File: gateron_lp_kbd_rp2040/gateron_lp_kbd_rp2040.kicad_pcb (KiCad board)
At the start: 2 copper layers, 234.5 x 116.5 mm, 306 parts, among them J1 TYPE-C-31-M-12, J2 Battery JST-SH, Q1 DMG3415U, SW1 KS-33, SW10 KS-33, SW11 KS-33, SW12 KS-33, SW13 KS-33, SW14 KS-33, SW15 KS-33, SW16 KS-33, SW17 KS-33, SW18 KS-33, SW19 KS-33, SW2 KS-33, SW20 KS-33, SW21 KS-33, SW22 KS-33, SW23 KS-33, SW24 KS-33, SW25 KS-33, SW26 KS-33, SW27 KS-33, SW28 KS-33, SW29 KS-33, SW3 KS-33, SW30 KS-33, SW31 KS-33, SW32 KS-33, SW33 KS-33, SW34 KS-33, SW35 KS-33, SW36 KS-33, SW37 KS-33, SW38 KS-33, SW39 KS-33, SW4 KS-33, SW40 KS-33, SW41 KS-33, SW42 KS-33, SW43 KS-33, SW44 KS-33, SW45 KS-33, SW46 KS-33, SW47 KS-33, SW48 KS-33, SW49 KS-33, SW5 KS-33, SW50 KS-33, SW51 KS-33, SW52 KS-33, SW53 KS-33, SW54 KS-33, SW55 KS-33, SW56 KS-33, SW57 KS-33, SW58 KS-33, SW59 KS-33, SW6 KS-33, SW60 RESET, SW61 BOOTSEL, SW62 PWR MSK-12C02, SW7 KS-33, SW8 KS-33, SW9 KS-33, U1 RP2040, U2 MCP73831, U3 AP2112K-3.3, U4 USBLC6-2SC6, U5 W25Q16JVUXIQ, U6 CYW43439, U7 SN74AHCT1G125DBVR, Y1 12MHz, Y2 37.4MHz

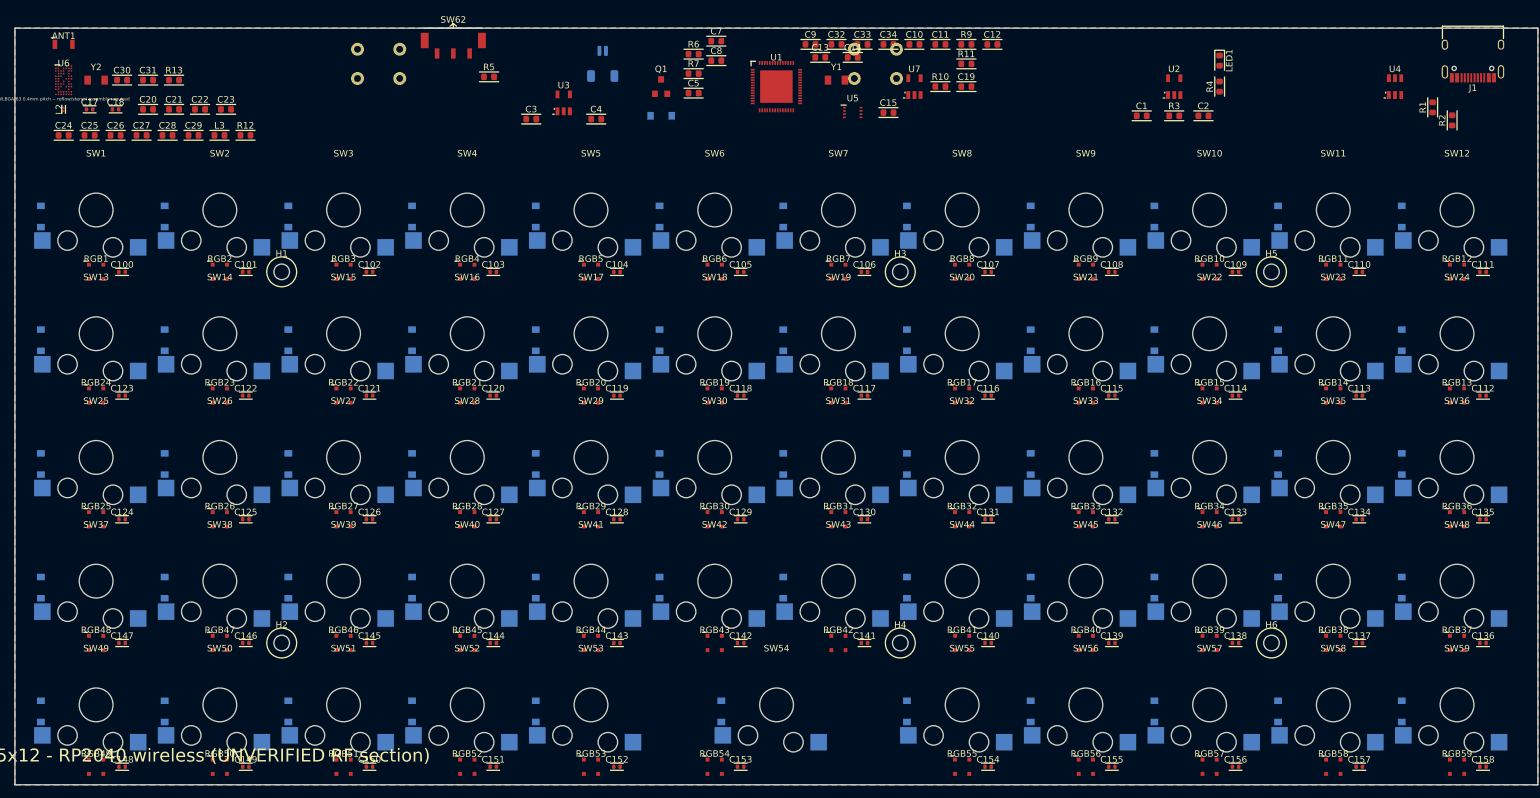
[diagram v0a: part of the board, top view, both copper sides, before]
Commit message: Add RP2040 board routing engine, reverse-mount LED redesign, and 3D models
- New route_kbd_rp2040.py: deterministic + A*-hybrid autorouter for the
  RP2040 variant. Hand-routes the congested ROW/COL matrix fanout and
  QSPI north strip net-by-net (verified against the real clearance
  checker), falls back to generic A* elsewhere, and heals remaining
  gaps in a final pass.
- Redesigned the per-key RGB LED footprint (fp_sk6812mini) to a real
  reverse-mount part on B.Cu with a light-transmission cutout, matching
  a verified KiCad reference footprint instead of a hand-derived one.
- Added 3D models to ~15 footprints across both board variants (via
  add_3d.py for the ESP32 variant, inline `model()` blocks for RP2040)
  and synced datasheets for real part verification.
- Fixed several real bugs surfaced while routing: VSYS's per-LED
  routing referenced the wrong pin after the LED footprint redesign
  (silently trying to via into GND on all 59 LEDs); the matching
  per-LED decoupling caps sat in the ~0mm gap between the LED's own
  cutout and the next row's switch leg hole; C33 was placed closer to
  BOOTSEL's through-hole pad than any trace could legally clear;
  BOOTSEL's own switch had two same-named leg pads that were never
  wired together; VBAT_SENSE's escape route was getting walled off by
  whichever of XIN/XOUT happened to route first.
- Board currently routes cleanly except for a known cluster of nets
  (+3V3, DVDD, QSPI_SCLK/SD2/SD3, RGB_GPIO, USB_DM/DP, VREG_VIN) all
  bottlenecked by the same over-saturated escape corridor next to U1 --
  next up for a dedicated deterministic-routing pass.

Co-Authored-By: Claude Sonnet 5 <noreply@anthropic.com>
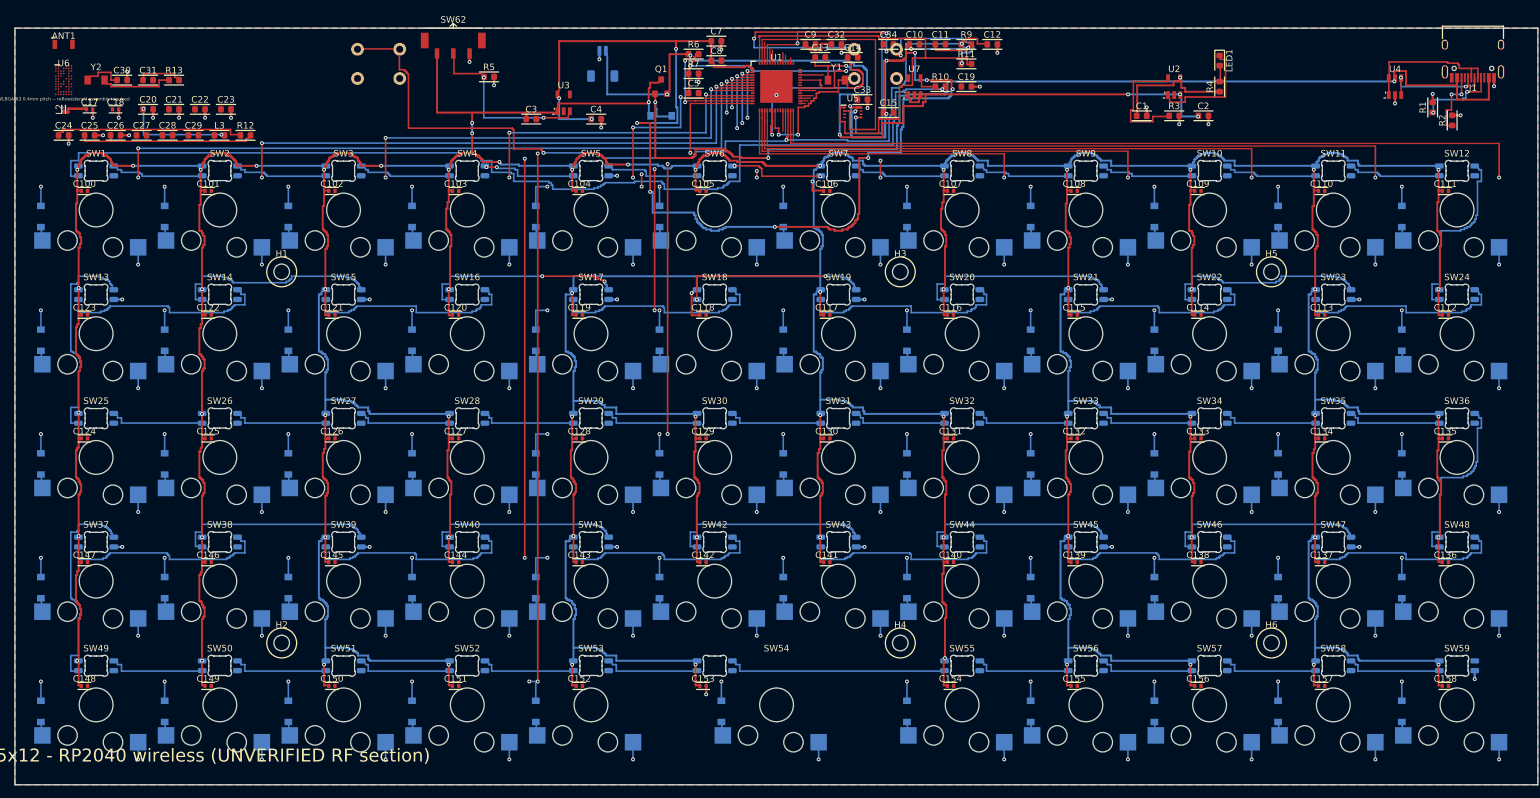
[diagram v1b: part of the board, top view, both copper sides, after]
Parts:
- RGB1, RGB10, RGB11, RGB12, RGB13, RGB14, RGB15, RGB16, RGB17, RGB18, RGB19, RGB2, RGB20, RGB21, RGB22, RGB23, RGB24, RGB25, RGB26, RGB27, RGB28, RGB29, RGB3, RGB30, RGB31, RGB32, RGB33, RGB34, RGB35, RGB36, RGB37, RGB38, RGB39, RGB4, RGB40, RGB41, RGB42, RGB43, RGB44, RGB45, RGB46, RGB47, RGB48, RGB49, RGB5, RGB50, RGB51, RGB52, RGB53, RGB54, RGB55, RGB56, RGB57, RGB58, RGB59, RGB6, RGB7, RGB8, RGB9: moved to B.Cu
- moved RGB13 15.6 mm to (259.6, 63.0), turned to 180 degrees
- moved RGB14 15.6 mm to (240.5, 63.0), turned to 180 degrees
- moved RGB15 15.6 mm to (221.4, 63.0), turned to 180 degrees
- moved RGB16 15.6 mm to (202.4, 63.0), turned to 180 degrees
- moved RGB17 15.6 mm to (183.3, 63.0), turned to 180 degrees
- moved RGB18 15.6 mm to (164.3, 63.0), turned to 180 degrees
- moved RGB19 15.6 mm to (145.2, 63.0), turned to 180 degrees
- moved RGB20 15.6 mm to (126.2, 63.0), turned to 180 degrees
- moved RGB21 15.6 mm to (107.2, 63.0), turned to 180 degrees
- moved RGB22 15.6 mm to (88.1, 63.0), turned to 180 degrees
- moved RGB23 15.6 mm to (69.0, 63.0), turned to 180 degrees
- moved RGB24 15.6 mm to (50.0, 63.0), turned to 180 degrees
- moved RGB1 15.5 mm to (50.0, 44.0), turned to 180 degrees
- moved RGB10 15.5 mm to (221.4, 44.0), turned to 180 degrees
- moved RGB11 15.5 mm to (240.5, 44.0), turned to 180 degrees
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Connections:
- RGB1 pad 1: VSYS -> GND
- RGB1 pad 3: GND -> VSYS
- RGB10 pad 1: VSYS -> GND
- RGB10 pad 3: GND -> VSYS
- RGB11 pad 1: VSYS -> GND
- RGB11 pad 3: GND -> VSYS
- RGB12 pad 1: VSYS -> GND
- RGB12 pad 3: GND -> VSYS
- RGB13 pad 1: VSYS -> GND
- RGB13 pad 3: GND -> VSYS
- RGB14 pad 1: VSYS -> GND
- RGB14 pad 3: GND -> VSYS
- RGB15 pad 1: VSYS -> GND
- RGB15 pad 3: GND -> VSYS
- RGB16 pad 1: VSYS -> GND
- RGB16 pad 3: GND -> VSYS
- RGB17 pad 1: VSYS -> GND
- RGB17 pad 3: GND -> VSYS
- RGB18 pad 1: VSYS -> GND
- RGB18 pad 3: GND -> VSYS
- RGB19 pad 1: VSYS -> GND
- RGB19 pad 3: GND -> VSYS
- RGB2 pad 1: VSYS -> GND
- RGB2 pad 3: GND -> VSYS
- RGB20 pad 1: VSYS -> GND
- RGB20 pad 3: GND -> VSYS
- RGB21 pad 1: VSYS -> GND
- RGB21 pad 3: GND -> VSYS
- RGB22 pad 1: VSYS -> GND
- RGB22 pad 3: GND -> VSYS
- RGB23 pad 1: VSYS -> GND
- RGB23 pad 3: GND -> VSYS
- RGB24 pad 1: VSYS -> GND
- RGB24 pad 3: GND -> VSYS
- RGB25 pad 1: VSYS -> GND
- RGB25 pad 3: GND -> VSYS
- RGB26 pad 1: VSYS -> GND
- RGB26 pad 3: GND -> VSYS
- RGB27 pad 1: VSYS -> GND
- RGB27 pad 3: GND -> VSYS
- RGB28 pad 1: VSYS -> GND
- RGB28 pad 3: GND -> VSYS
- RGB29 pad 1: VSYS -> GND
- RGB29 pad 3: GND -> VSYS
- RGB3 pad 1: VSYS -> GND
- RGB3 pad 3: GND -> VSYS
- RGB30 pad 1: VSYS -> GND
- RGB30 pad 3: GND -> VSYS
- RGB31 pad 1: VSYS -> GND
- RGB31 pad 3: GND -> VSYS
- RGB32 pad 1: VSYS -> GND
- RGB32 pad 3: GND -> VSYS
- RGB33 pad 1: VSYS -> GND
- RGB33 pad 3: GND -> VSYS
- RGB34 pad 1: VSYS -> GND
- RGB34 pad 3: GND -> VSYS
- RGB35 pad 1: VSYS -> GND
- RGB35 pad 3: GND -> VSYS
- RGB36 pad 1: VSYS -> GND
- RGB36 pad 3: GND -> VSYS
- RGB37 pad 1: VSYS -> GND
- RGB37 pad 3: GND -> VSYS
- RGB38 pad 1: VSYS -> GND
- RGB38 pad 3: GND -> VSYS
- RGB39 pad 1: VSYS -> GND
- RGB39 pad 3: GND -> VSYS
- RGB4 pad 1: VSYS -> GND
- RGB4 pad 3: GND -> VSYS
- RGB40 pad 1: VSYS -> GND
- RGB40 pad 3: GND -> VSYS
- RGB41 pad 1: VSYS -> GND
- RGB41 pad 3: GND -> VSYS
- RGB42 pad 1: VSYS -> GND
- RGB42 pad 3: GND -> VSYS
- RGB43 pad 1: VSYS -> GND
- RGB43 pad 3: GND -> VSYS
- RGB44 pad 1: VSYS -> GND
- RGB44 pad 3: GND -> VSYS
- RGB45 pad 1: VSYS -> GND
- RGB45 pad 3: GND -> VSYS
- RGB46 pad 1: VSYS -> GND
- RGB46 pad 3: GND -> VSYS
- RGB47 pad 1: VSYS -> GND
- RGB47 pad 3: GND -> VSYS
- RGB48 pad 1: VSYS -> GND
- RGB48 pad 3: GND -> VSYS
- RGB49 pad 1: VSYS -> GND
- RGB49 pad 3: GND -> VSYS
- RGB5 pad 1: VSYS -> GND
- RGB5 pad 3: GND -> VSYS
- RGB50 pad 1: VSYS -> GND
- RGB50 pad 3: GND -> VSYS
- RGB51 pad 1: VSYS -> GND
- RGB51 pad 3: GND -> VSYS
- RGB52 pad 1: VSYS -> GND
- RGB52 pad 3: GND -> VSYS
- RGB53 pad 1: VSYS -> GND
- RGB53 pad 3: GND -> VSYS
- RGB54 pad 1: VSYS -> GND
- RGB54 pad 3: GND -> VSYS
- RGB55 pad 1: VSYS -> GND
- RGB55 pad 3: GND -> VSYS
- RGB56 pad 1: VSYS -> GND
- RGB56 pad 3: GND -> VSYS
- RGB57 pad 1: VSYS -> GND
- RGB57 pad 3: GND -> VSYS
- RGB58 pad 1: VSYS -> GND
- RGB58 pad 3: GND -> VSYS
- RGB59 pad 1: VSYS -> GND
- RGB59 pad 3: GND -> VSYS
- RGB6 pad 1: VSYS -> GND
- RGB6 pad 3: GND -> VSYS
- RGB7 pad 1: VSYS -> GND
- RGB7 pad 3: GND -> VSYS
- RGB8 pad 1: VSYS -> GND
- RGB8 pad 3: GND -> VSYS
- RGB9 pad 1: VSYS -> GND
- RGB9 pad 3: GND -> VSYS
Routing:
- net VSYS: track 0.00 -> 1444.5 mm, vias 0 -> 68
- net ROW4: track 0.00 -> 368.9 mm, vias 0 -> 15
- net ROW3: track 0.00 -> 356.0 mm, vias 0 -> 16
- net ROW2: track 0.00 -> 315.3 mm, vias 0 -> 16
- net ROW1: track 0.00 -> 298.7 mm, vias 0 -> 16
- net ROW0: track 0.00 -> 282.0 mm, vias 0 -> 16
- net +3V3: track 0.00 -> 243.5 mm, vias 0 -> 16
- net COL11: track 0.00 -> 222.3 mm, vias 0 -> 6
- net COL0: track 0.00 -> 212.1 mm, vias 0 -> 8
- net COL10: track 0.00 -> 206.8 mm, vias 0 -> 6
- net COL1: track 0.00 -> 192.6 mm, vias 0 -> 8
- net COL9: track 0.00 -> 188.2 mm, vias 0 -> 6
- net VBUS: track 0.00 -> 186.7 mm, vias 0 -> 4
- net COL2: track 0.00 -> 173.2 mm, vias 0 -> 8
- net COL8: track 0.00 -> 169.5 mm, vias 0 -> 6
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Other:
- copper layers 2 -> 4

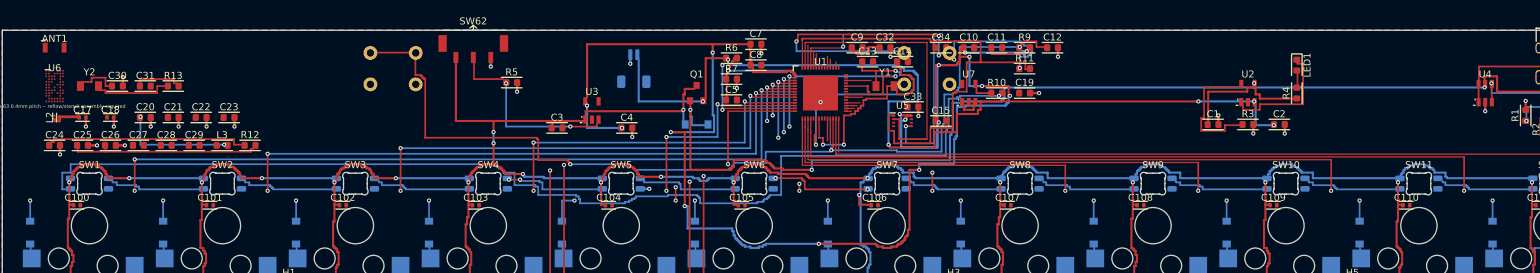
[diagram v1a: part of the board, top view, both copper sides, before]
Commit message: Route +3V3/DVDD orphan pins via In1/In2 expressways
Fixes 7 of 8 remaining +3V3/DVDD U1-pin orphans (pins 10, 22, 33, 42,
43, 48, 49, and DVDD pin 23) by hand-placing short F-layer escape jogs
into In1/In2 highway crossings instead of relying on the generic A*
router, which kept losing to 0.4mm-pitch pin congestion near U1.

+3V3 is now fully connected. DVDD's C32->C33 hop and pin 10's own long
F-layer escape wall still need work -- the latter is currently
trapping XIN's and QSPI_SS's own escape routes (regression, still
being chased).

Co-Authored-By: Claude Sonnet 5 <noreply@anthropic.com>
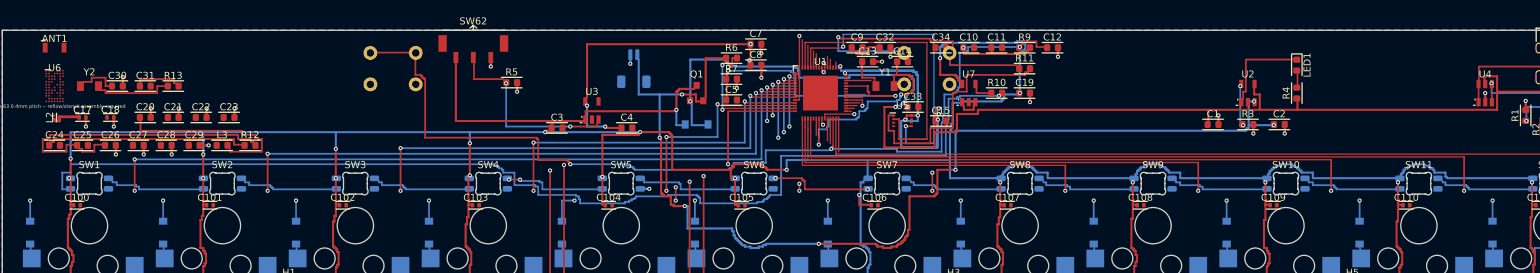
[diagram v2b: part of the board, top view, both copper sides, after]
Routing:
- net VSYS: track 1444.5 -> 1512.8 mm, vias 68 -> 69
- net XIN: track 40.0 -> 7.30 mm, vias 2 -> 0
- net QSPI_SS: track 71.1 -> 39.1 mm
- net BAT+: track 133.0 -> 157.2 mm, vias 6 -> 7
- net BOOTSEL: track 63.5 -> 41.5 mm, vias 5 -> 1
- net CYW_PA_VDD: track 27.9 -> 45.0 mm
- net DVDD: track 5.33 -> 18.9 mm, vias 0 -> 2
- net PROG: track 18.7 -> 6.13 mm, vias 0 -> 2
- net CYW_VDD1P5: track 16.3 -> 27.5 mm, vias 2 -> 0
- net +3V3: track 243.5 -> 235.3 mm, vias 16 -> 17
- net STAT: track 17.3 -> 13.5 mm
- net VBUS: track 186.7 -> 189.1 mm, vias 4 -> 2
- net XOUT: track 33.4 -> 34.0 mm

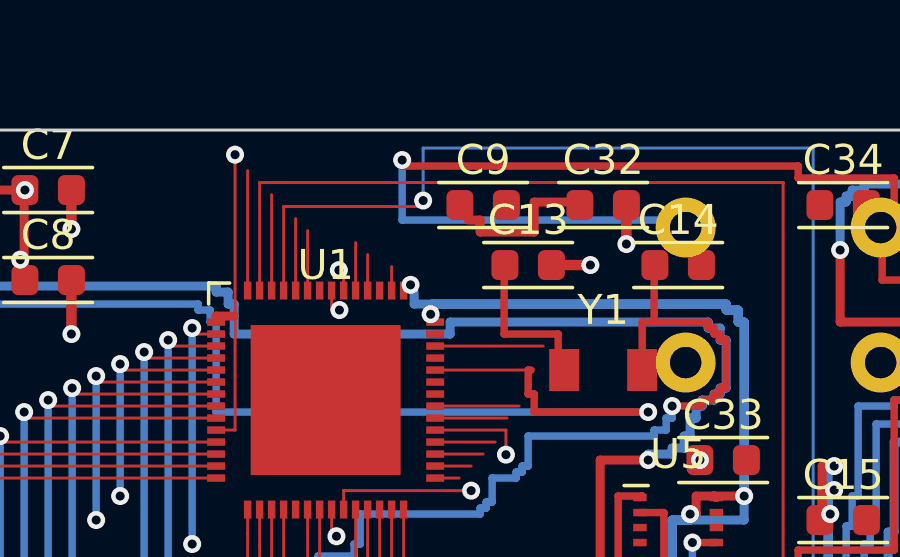
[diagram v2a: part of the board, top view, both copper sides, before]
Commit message: Fix DVDD's C33->U1 pins 45/50 hop, completing the +3V3/DVDD refactor
The direct route from C33's via to U1's N-side pins 45/50 crosses a
pocket (x=152-168, y=29-36) saturated with other nets' own vias
(+3V3, QSPI_SD0, VBAT_SENSE, XOUT, a GND keepout) -- no lane at any Y
in that band clears on any layer. Routed around it instead, joining
the existing C32->C33 In1 highway's y=23.5 lane at y=23.7 (23.5 itself
is blocked by a BOOTSEL via 0.5mm away).

DVDD and +3V3 are now both fully connected.

Co-Authored-By: Claude Sonnet 5 <noreply@anthropic.com>
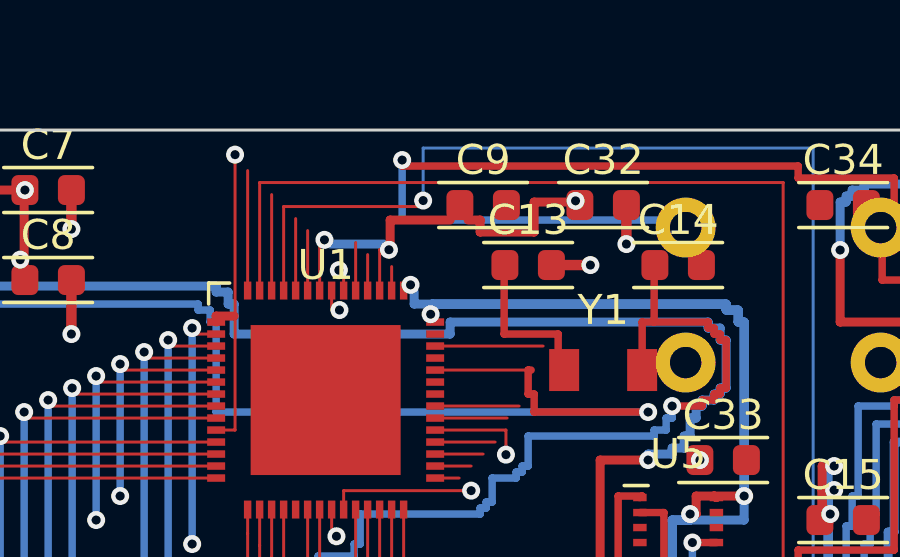
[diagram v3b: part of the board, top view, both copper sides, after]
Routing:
- net DVDD: track 18.9 -> 47.3 mm, vias 2 -> 5
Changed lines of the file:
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@@
   (segment (start 161.700 24.400) (end 163.300 24.400) (width 0.3) (layer "F.Cu") (net 18))
   (segment (start 163.225 24.500) (end 163.300 24.400) (width 0.3) (layer "F.Cu") (net 18))
+  (segment (start 163.225 24.500) (end 163.080 24.500) (width 0.1) (layer "F.Cu") (net 18))
+  (segment (start 163.080 24.500) (end 163.080 24.360) (width 0.1) (layer "F.Cu") (net 18))
+  (segment (start 163.080 24.360) (end 163.080 23.500) (width 0.3) (layer "In1.Cu") (net 18))
+  (segment (start 163.080 23.500) (end 170.000 23.500) (width 0.3) (layer "In1.Cu") (net 18))
+  (segment (start 170.000 23.500) (end 170.000 33.000) (width 0.3) (layer "In1.Cu") (net 18))
+  (segment (start 170.000 33.000) (end 167.225 33.000) (width 0.3) (layer "In1.Cu") (net 18))
+  (segment (start 156.550 27.350) (end 156.550 25.990) (width 0.1) (layer "F.Cu") (net 18))
+  (segment (start 156.550 25.990) (end 156.860 25.990) (width 0.1) (layer "F.Cu") (net 18))
+  (segment (start 154.550 27.350) (end 154.550 25.660) (width 0.1) (layer "F.Cu") (net 18))
+  (segment (start 154.550 25.660) (end 154.710 25.660) (width 0.1) (layer "F.Cu") (net 18))
   (segment (start 175.300 32.800) (end 175.300 33.400) (width 0.3) (layer "F.Cu") (net 1))
   (segment (start 175.300 33.400) (end 176.700 33.400) (width 0.3) (layer "F.Cu") (net 1))
@@
   (segment (start 168.700 34.200) (end 167.700 34.200) (width 0.3) (layer "F.Cu") (net 2))
   (segment (start 167.775 34.250) (end 167.700 34.200) (width 0.3) (layer "F.Cu") (net 2))
+  (segment (start 156.900 25.800) (end 156.900 25.000) (width 0.3) (layer "F.Cu") (net 18))
+  (segment (start 156.900 25.000) (end 158.900 25.000) (width 0.3) (layer "F.Cu") (net 18))
+  (segment (start 154.900 25.800) (end 156.700 25.800) (width 0.3) (layer "B.Cu") (net 18))
   (segment (start 91.100 25.200) (end 95.900 25.200) (width 0.25) (layer "F.Cu") (net 15))
   (segment (start 115.900 36.400) (end 115.300 36.400) (width 0.3) (layer "F.Cu") (net 4))
@@
   (via (at 118.900 41.200) (size 0.6) (drill 0.3) (layers "F.Cu" "B.Cu") (net 15))
   (via (at 157.300 23.000) (size 0.6) (drill 0.3) (layers "F.Cu" "B.Cu") (net 16))
+  (via (at 163.080 24.360) (size 0.6) (drill 0.3) (layers "F.Cu" "B.Cu") (net 18))
+  (via (at 156.860 25.990) (size 0.6) (drill 0.3) (layers "F.Cu" "B.Cu") (net 18))
+  (via (at 154.710 25.660) (size 0.6) (drill 0.3) (layers "F.Cu" "B.Cu") (net 18))
   (via (at 171.900 26.000) (size 0.6) (drill 0.3) (layers "F.Cu" "B.Cu") (net 4))
   (via (at 183.300 31.000) (size 0.6) (drill 0.3) (layers "F.Cu" "B.Cu") (net 4))
